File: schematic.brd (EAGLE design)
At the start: 108.2 x 139.7 mm, 134 parts, among them IC1 AD8015, IC2 AD8015, IC3 AD8015, IC4 AD8015

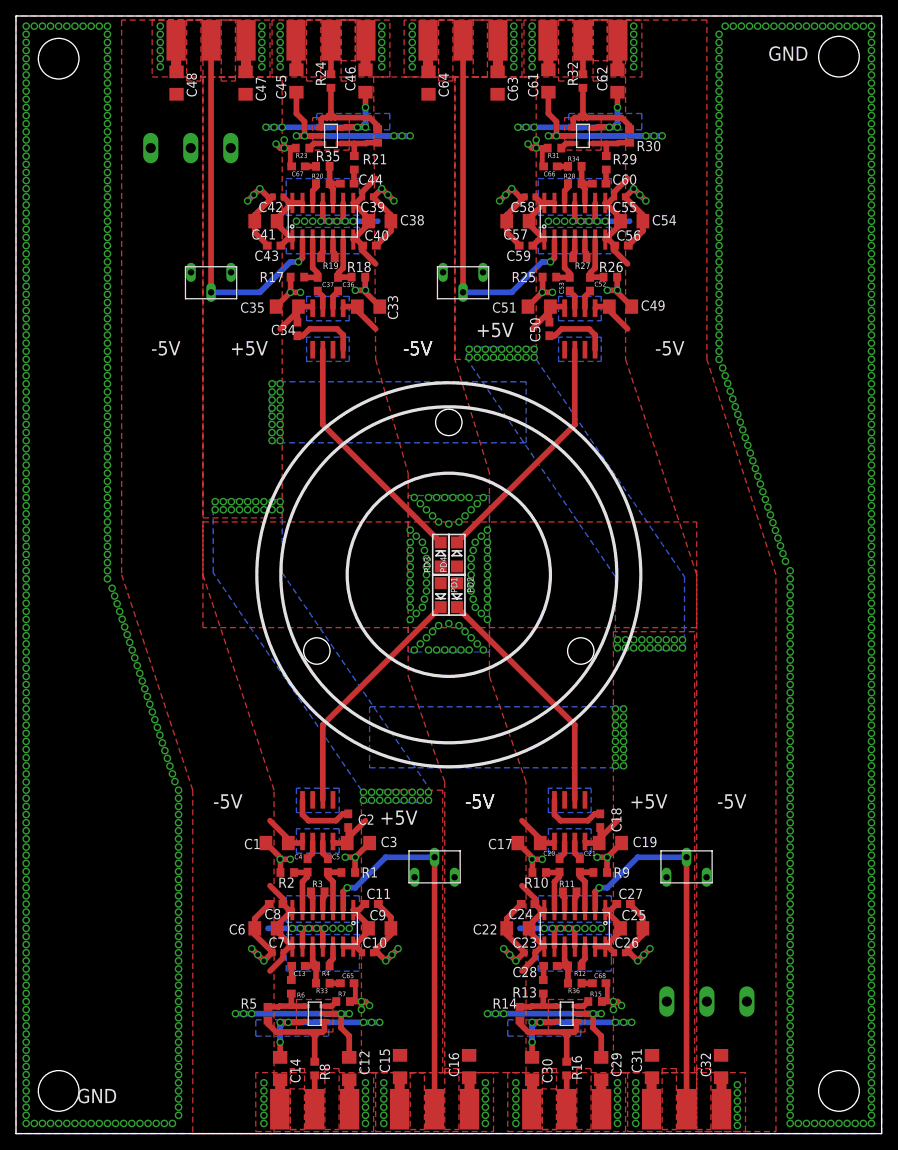
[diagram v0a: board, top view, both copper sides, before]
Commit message: Added bypass caps
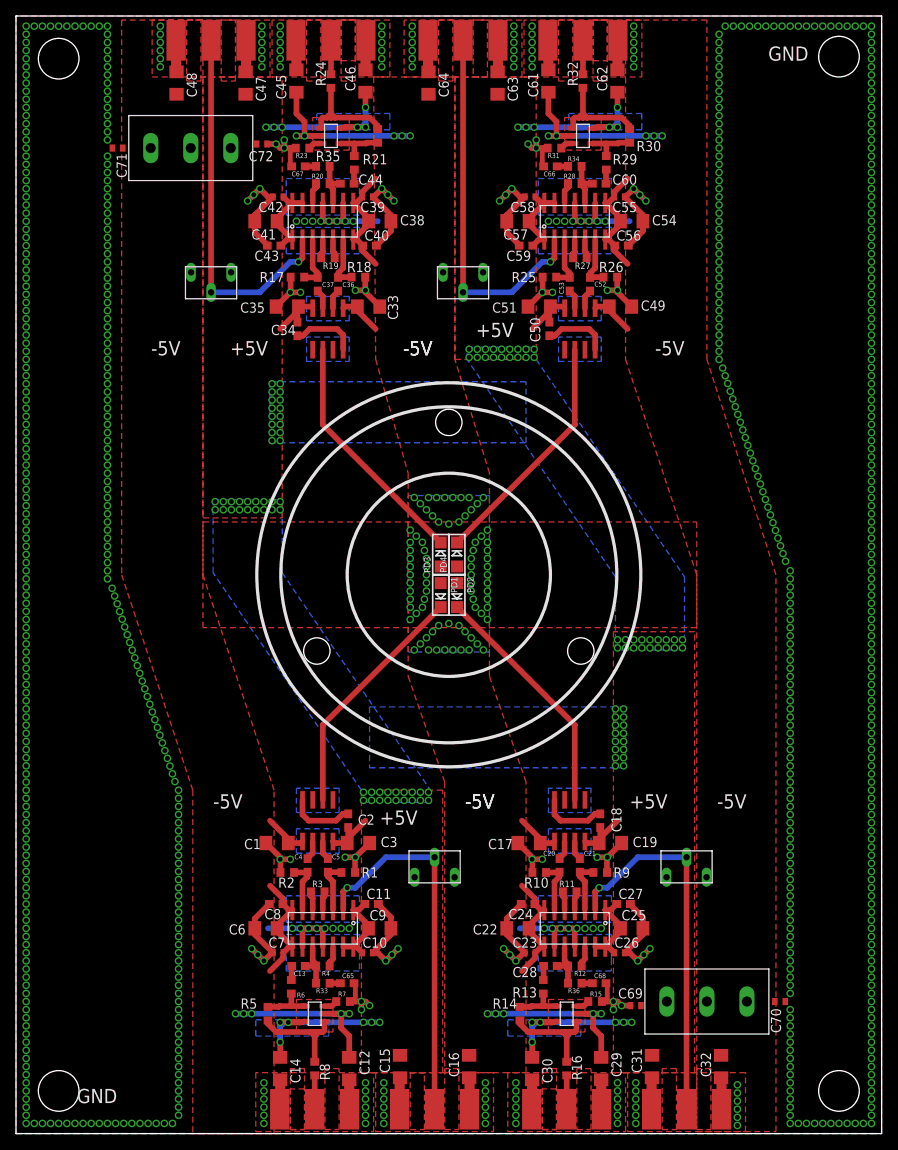
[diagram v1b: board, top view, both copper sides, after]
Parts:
- added C69, C70, C71, C72: 0.1uF, rcl:C0402
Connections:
- net +5V: now also C69.1, C72.1
- net -5V: now also C70.1, C71.1
- net GND: now also C69.2, C70.2, C71.2, C72.2
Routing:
- net GND: track 285.6 -> 287.9 mm, vias 778 -> 776
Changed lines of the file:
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@@
 <attribute name="VALUE" x="72.263" y="16.891" size="1.27" layer="27"/>
+</element>
+<element name="C69" library="rcl" package="C0402" value="0.1uF" x="77.47" y="16.002" smashed="yes" rot="R180">
+<attribute name="NAME" x="78.359" y="18.161" size="1.27" layer="25" rot="R180"/>
+<attribute name="VALUE" x="78.105" y="17.907" size="1.27" layer="27" rot="R180"/>
+</element>
+<element name="C70" library="rcl" package="C0402" value="0.1uF" x="95.504" y="16.51" smashed="yes">
+<attribute name="NAME" x="95.631" y="12.573" size="1.27" layer="25" rot="R90"/>
+<attribute name="VALUE" x="94.869" y="14.605" size="1.27" layer="27"/>
+</element>
+<element name="C71" library="rcl" package="C0402" value="0.1uF" x="12.7" y="123.19" smashed="yes" rot="R180">
+<attribute name="NAME" x="12.573" y="122.555" size="1.27" layer="25" rot="R270"/>
+<attribute name="VALUE" x="13.335" y="125.095" size="1.27" layer="27" rot="R180"/>
+</element>
+<element name="C72" library="rcl" package="C0402" value="0.1uF" x="30.734" y="123.698" smashed="yes">
+<attribute name="NAME" x="29.083" y="121.539" size="1.27" layer="25"/>
+<attribute name="VALUE" x="30.099" y="121.793" size="1.27" layer="27"/>
 </element>
 </elements>
@@
 <via x="49.276" y="66.802" extent="1-16" drill="0.6"/>
 <via x="49.276" y="67.818" extent="1-16" drill="0.6"/>
+<contactref element="C70" pad="1"/>
+<contactref element="C71" pad="1"/>
 </signal>
 <signal name="+5V">
@@
 <via x="57.658" y="98.044" extent="1-16" drill="0.6"/>
 <via x="56.642" y="98.044" extent="1-16" drill="0.6"/>
+<contactref element="C69" pad="1"/>
+<contactref element="C72" pad="1"/>
 </signal>
 <signal name="N$3">
@@
 <via x="96.774" y="18.542" extent="1-16" drill="0.6"/>
 <via x="96.774" y="17.526" extent="1-16" drill="0.6"/>
-<via x="96.774" y="16.51" extent="1-16" drill="0.6"/>
 <via x="96.774" y="15.494" extent="1-16" drill="0.6"/>
 <via x="96.774" y="14.478" extent="1-16" drill="0.6"/>
@@
 <via x="11.43" y="121.158" extent="1-16" drill="0.6"/>
 <via x="11.43" y="122.174" extent="1-16" drill="0.6"/>
-<via x="11.43" y="123.19" extent="1-16" drill="0.6"/>
 <via x="11.43" y="124.206" extent="1-16" drill="0.6"/>
 <via x="11.43" y="125.222" extent="1-16" drill="0.6"/>
@@
 <via x="12.331484375" y="67.19641875" extent="1-16" drill="0.6"/>
 <via x="12.017525" y="68.16269375" extent="1-16" drill="0.6"/>
+<contactref element="C69" pad="2"/>
+<contactref element="C70" pad="2"/>
+<contactref element="C71" pad="2"/>
+<contactref element="C72" pad="2"/>
+<wire x1="76.82" y1="16.002" x2="75.692" y2="16.002" width="0.7112" layer="1"/>
+<wire x1="31.384" y1="123.698" x2="32.512" y2="123.698" width="0.7112" layer="1"/>
 </signal>
 <signal name="N$19">

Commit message: Fixed BNC package and updated schematic labels
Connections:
- net GND: now also U$10.4, U$10.5, U$14.4, U$14.5, U$15.4, U$15.5, U$19.4, U$19.5, U$20.4, U$20.5, U$4.4, U$4.5, U$5.4, U$5.5, U$9.4, U$9.5
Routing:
- net GND: vias 776 -> 772
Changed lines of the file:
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@@
 <via x="96.774" y="19.558" extent="1-16" drill="0.6"/>
 <via x="96.774" y="18.542" extent="1-16" drill="0.6"/>
-<via x="96.774" y="17.526" extent="1-16" drill="0.6"/>
-<via x="96.774" y="15.494" extent="1-16" drill="0.6"/>
 <via x="96.774" y="14.478" extent="1-16" drill="0.6"/>
 <via x="96.774" y="13.462" extent="1-16" drill="0.6"/>
@@
 <via x="11.43" y="120.142" extent="1-16" drill="0.6"/>
 <via x="11.43" y="121.158" extent="1-16" drill="0.6"/>
-<via x="11.43" y="122.174" extent="1-16" drill="0.6"/>
-<via x="11.43" y="124.206" extent="1-16" drill="0.6"/>
 <via x="11.43" y="125.222" extent="1-16" drill="0.6"/>
 <via x="11.43" y="126.238" extent="1-16" drill="0.6"/>
@@
 <wire x1="76.82" y1="16.002" x2="75.692" y2="16.002" width="0.7112" layer="1"/>
 <wire x1="31.384" y1="123.698" x2="32.512" y2="123.698" width="0.7112" layer="1"/>
+<contactref element="U$4" pad="5"/>
+<contactref element="U$4" pad="4"/>
+<contactref element="U$5" pad="5"/>
+<contactref element="U$5" pad="4"/>
+<contactref element="U$9" pad="5"/>
+<contactref element="U$9" pad="4"/>
+<contactref element="U$10" pad="5"/>
+<contactref element="U$10" pad="4"/>
+<contactref element="U$14" pad="5"/>
+<contactref element="U$14" pad="4"/>
+<contactref element="U$15" pad="5"/>
+<contactref element="U$15" pad="4"/>
+<contactref element="U$19" pad="5"/>
+<contactref element="U$19" pad="4"/>
+<contactref element="U$20" pad="5"/>
+<contactref element="U$20" pad="4"/>
 </signal>
 <signal name="N$19">
